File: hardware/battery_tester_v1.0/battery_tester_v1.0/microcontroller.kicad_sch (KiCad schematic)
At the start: 7 parts, among them IC4 PIC18F67J50, J1 USB_B, J2 MTA05-100

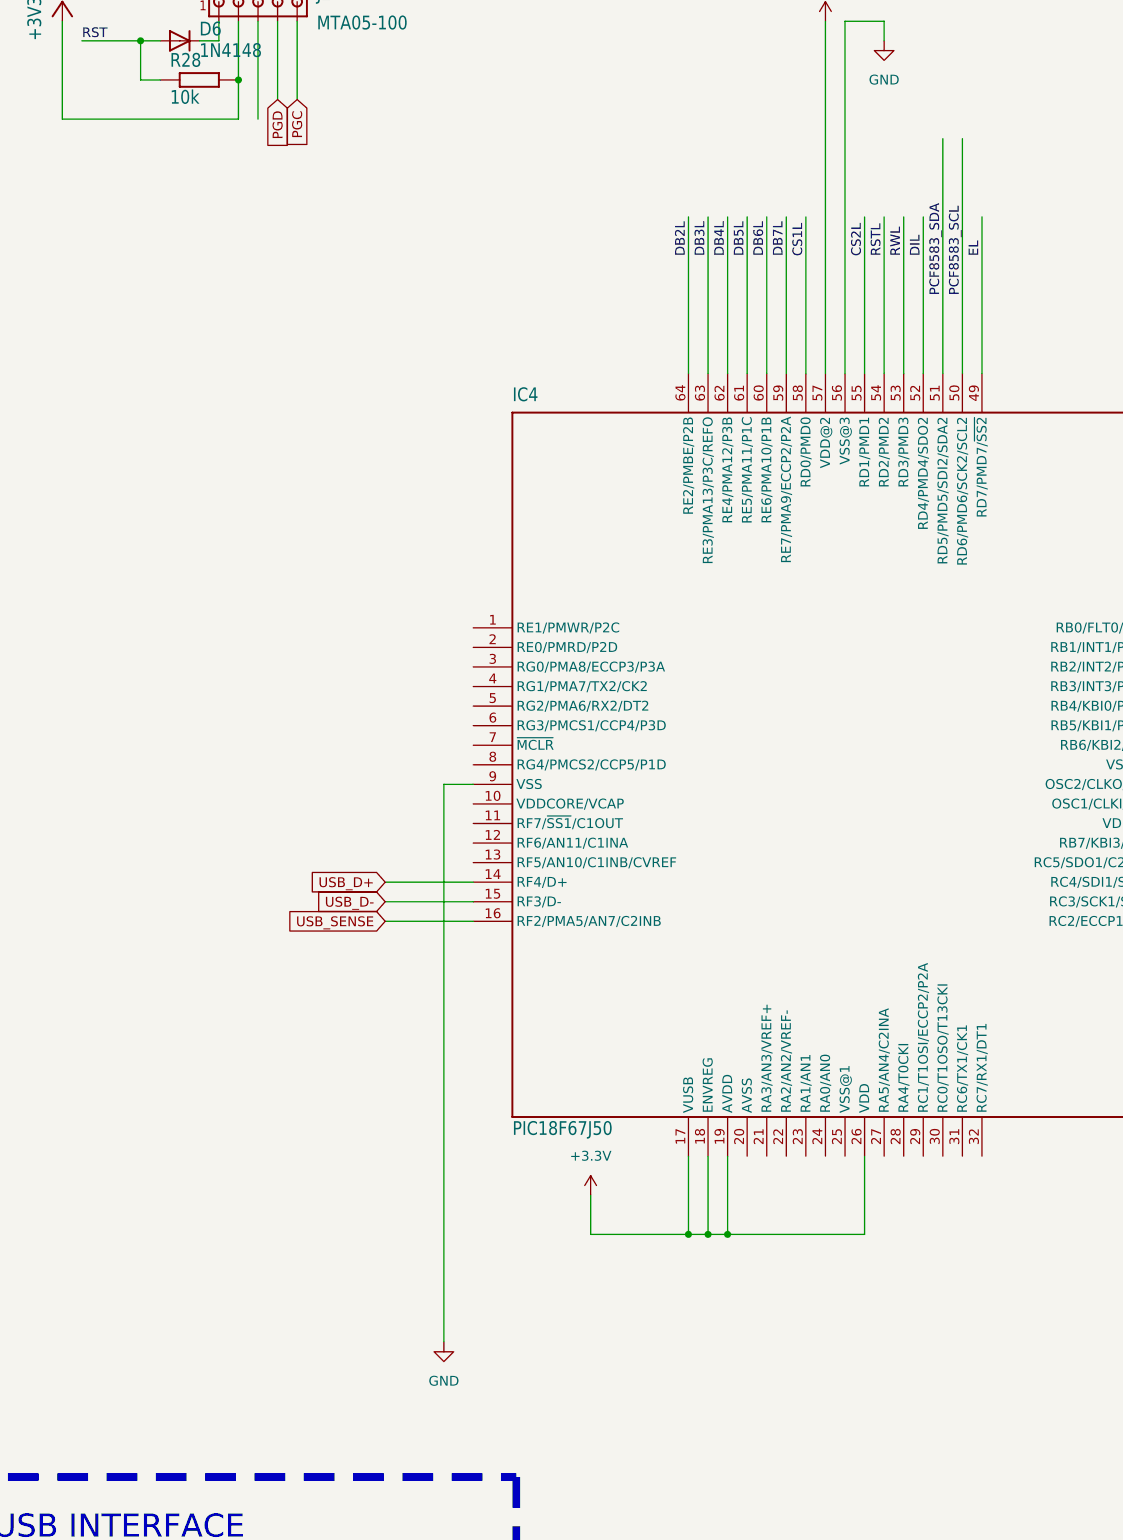
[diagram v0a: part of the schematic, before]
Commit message: update schematic
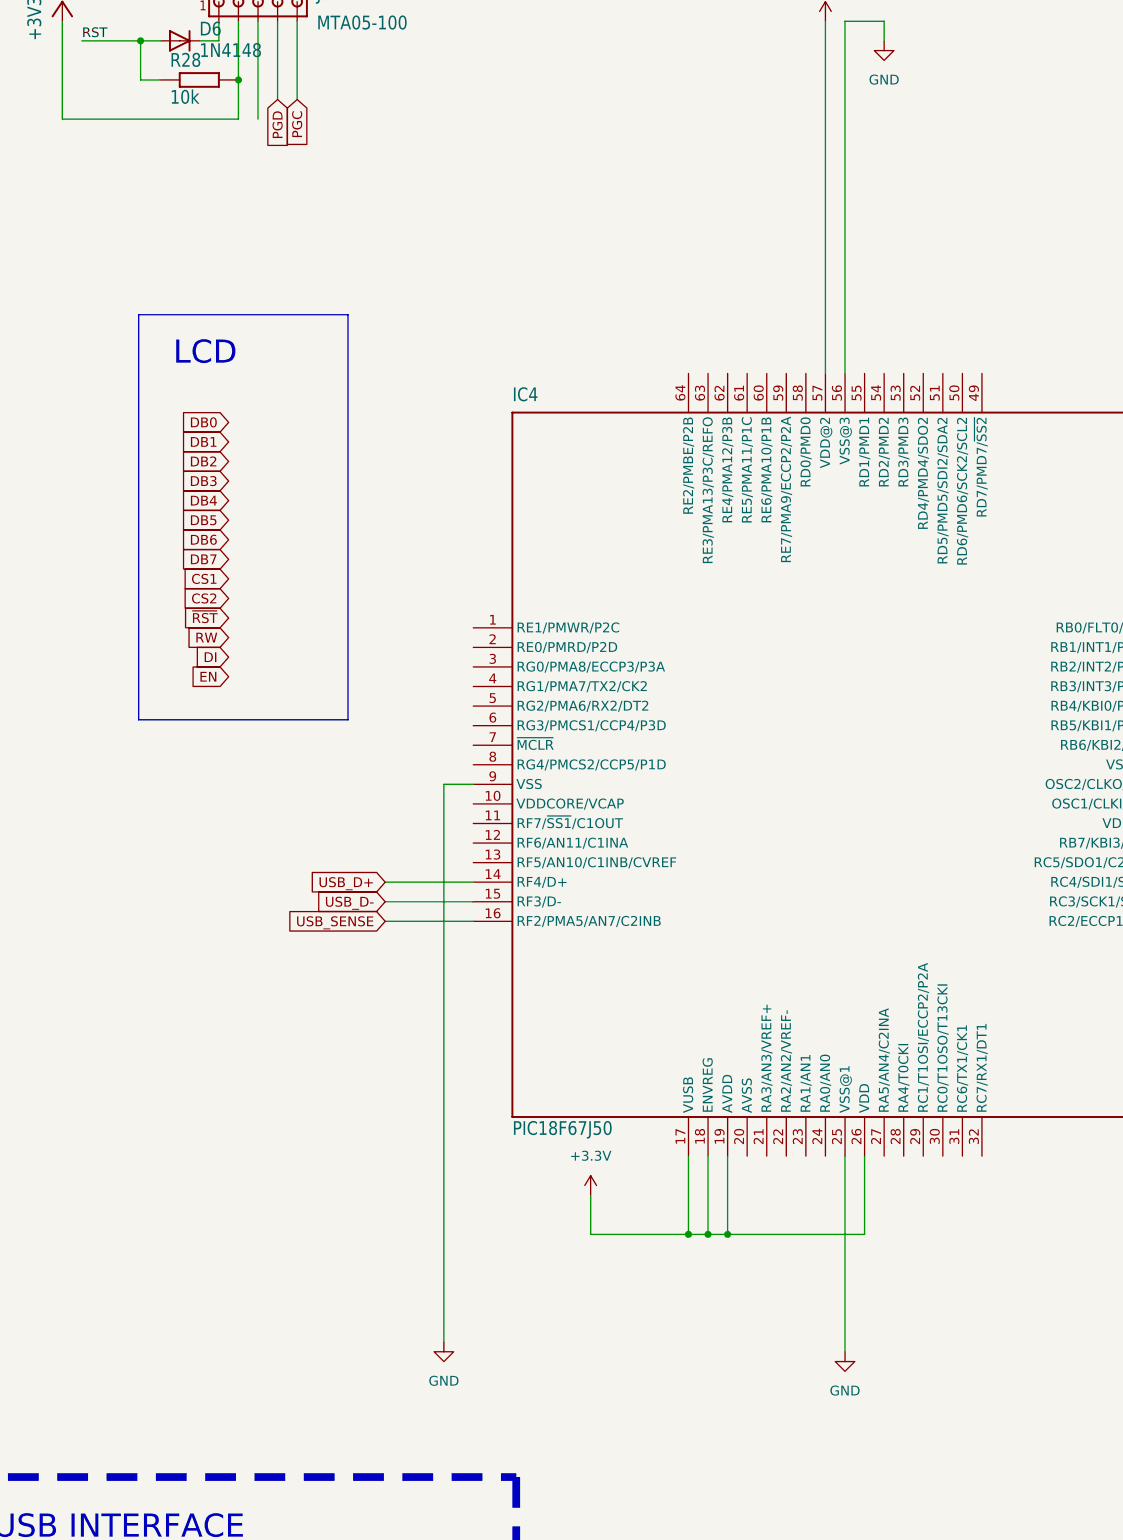
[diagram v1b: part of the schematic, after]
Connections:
- net GND: now also IC4.25 (VSS@1)
- net CS1L: no longer names the net of IC4.58 (RD0/PMD0)
- net CS2L: no longer names the net of IC4.55 (RD1/PMD1)
- net DB2L: no longer names the net of IC4.64 (RE2/PMBE/P2B)
- net DB3L: no longer names the net of IC4.63 (RE3/PMA13/P3C/REFO)
- net DB4L: no longer names the net of IC4.62 (RE4/PMA12/P3B)
- net DB5L: no longer names the net of IC4.61 (RE5/PMA11/P1C)
- net DB6L: no longer names the net of IC4.60 (RE6/PMA10/P1B)
- net DB7L: no longer names the net of IC4.59 (RE7/PMA9/ECCP2/P2A)
- net DIL: no longer names the net of IC4.52 (RD4/PMD4/SDO2)
- net EL: no longer names the net of IC4.49 (RD7/PMD7/~{SS2})
- net PCF8583_SCL: no longer names the net of IC4.50 (RD6/PMD6/SCK2/SCL2)
- net PCF8583_SDA: no longer names the net of IC4.51 (RD5/PMD5/SDI2/SDA2)
- net RSTL: no longer names the net of IC4.54 (RD2/PMD2)
- net RWL: no longer names the net of IC4.53 (RD3/PMD3)
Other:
- note added: "LCD"

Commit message: update lcd pcb
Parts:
- removed D6: 1N4148, centralaV2.2:SOD80C, symbol centralaV2.2-eagle-import:PMLL4150
- removed J2: MTA05-100, centralaV2.2:10X05MTA, symbol centralaV2.2-eagle-import:MTA05-100
- removed R28: 10k, centralaV2.2:R0805, symbol centralaV2.2-eagle-import:R-EU_R0805
- added C?: 470u/10V, Capacitor_THT:CP_Radial_D8.0mm_P3.80mm, symbol Device:C_Polarized
- added C?: 100n, Capacitor_SMD:C_0805_2012Metric_Pad1.18x1.45mm_HandSolder, symbol Device:C
- added J2: ICP, symbol Connector_Generic:Conn_01x06
- added LCD1: RG12864B-BIW-V, symbol My-Lib:RG12864B-BIW-V
- added Q?: BC817, Package_TO_SOT_SMD:SOT-23, symbol Transistor_BJT:BC817
- added R10: 10k, symbol Device:R
- added R? (x2): 10k, Resistor_SMD:R_0805_2012Metric, symbol Device:R
- added R? (x2): R, Resistor_SMD:R_1206_3216Metric, symbol Device:R
- added R? (x2): R, Resistor_SMD:R_0805_2012Metric_Pad1.20x1.40mm_HandSolder, symbol Device:R
- added RV?: 10k, Potentiometer_THT:Potentiometer_ACP_CA9-V10_Vertical_Hole, symbol Device:R_Potentiometer
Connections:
- net +3.3V: now also J2.2 (Pin_2), R10.2
- net CS1: now also IC4.58 (RD0/PMD0), LCD1.12 (CS1)
- net CS2: now also IC4.55 (RD1/PMD1), LCD1.13 (CS2)
- net DB0: now also IC4.2 (RE0/PMRD/P2D), LCD1.4 (DB0)
- net DB1: now also IC4.1 (RE1/PMWR/P2C), LCD1.5 (DB1)
- net DB2: now also IC4.64 (RE2/PMBE/P2B), LCD1.6 (DB2)
- net DB3: now also IC4.63 (RE3/PMA13/P3C/REFO), LCD1.7 (DB3)
- net DB4: now also IC4.62 (RE4/PMA12/P3B), LCD1.8 (DB4)
- net DB5: now also IC4.61 (RE5/PMA11/P1C), LCD1.9 (DB5)
- net DB6: now also IC4.60 (RE6/PMA10/P1B), LCD1.10 (DB6)
- net DB7: now also IC4.59 (RE7/PMA9/ECCP2/P2A), LCD1.11 (DB7)
- net DI: now also IC4.53 (RD3/PMD3), LCD1.16 (D/~{I})
- net EN: now also IC4.54 (RD2/PMD2), LCD1.17 (E)
- net GND: now also C?.2, C?.2, J2.3 (Pin_3), LCD1.15 (R/~{W}), LCD1.2 (VSS), Q?.2 (E), R?.1
- net PGC: now also J2.5 (Pin_5)
- net PGD: now also J2.4 (Pin_4)
- net RW: now also IC4.52 (RD4/PMD4/SDO2)
- net ~{RST}: now also IC4.51 (RD5/PMD5/SDI2/SDA2), IC4.7 (~{MCLR}), J2.1 (Pin_1), LCD1.14 (~{RST}), R10.1
- net ADC_DISCHARGE_CURRENT: now reaches IC4.24 (RA0/AN0)
- net LCD_BACKLIGHT: now reaches IC4.50 (RD6/PMD6/SCK2/SCL2)
- net LCD_BACKLIGHT: now also R?.1, R?.2
- new net: LCD1.18 (VEE), R?.2, RV?.1
- new net: LCD1.3 (VO), R?.1, R?.2, RV?.2
- new net: Q?.1 (B), R?.2
- new net: LCD1.20 (K), R?.1, R?.1
- new net: Q?.3 (C), R?.2, R?.2
- new net +5V: C?.1, C?.1, LCD1.1 (VDD), LCD1.19 (A), R?.1, RV?.3
- new net DBG_UART: J2.6 (Pin_6)
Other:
- note removed: "LCD"
- note removed: "PIC ISP connector"
- moved on the sheet: J1, R1, R2
